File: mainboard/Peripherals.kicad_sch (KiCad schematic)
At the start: 30 parts, among them IC1101 PCAL6416AHF, IC1102 TMP100, IC1103 RV-8263-C8, IC506 PCA9306JK, Q1101 BSS138

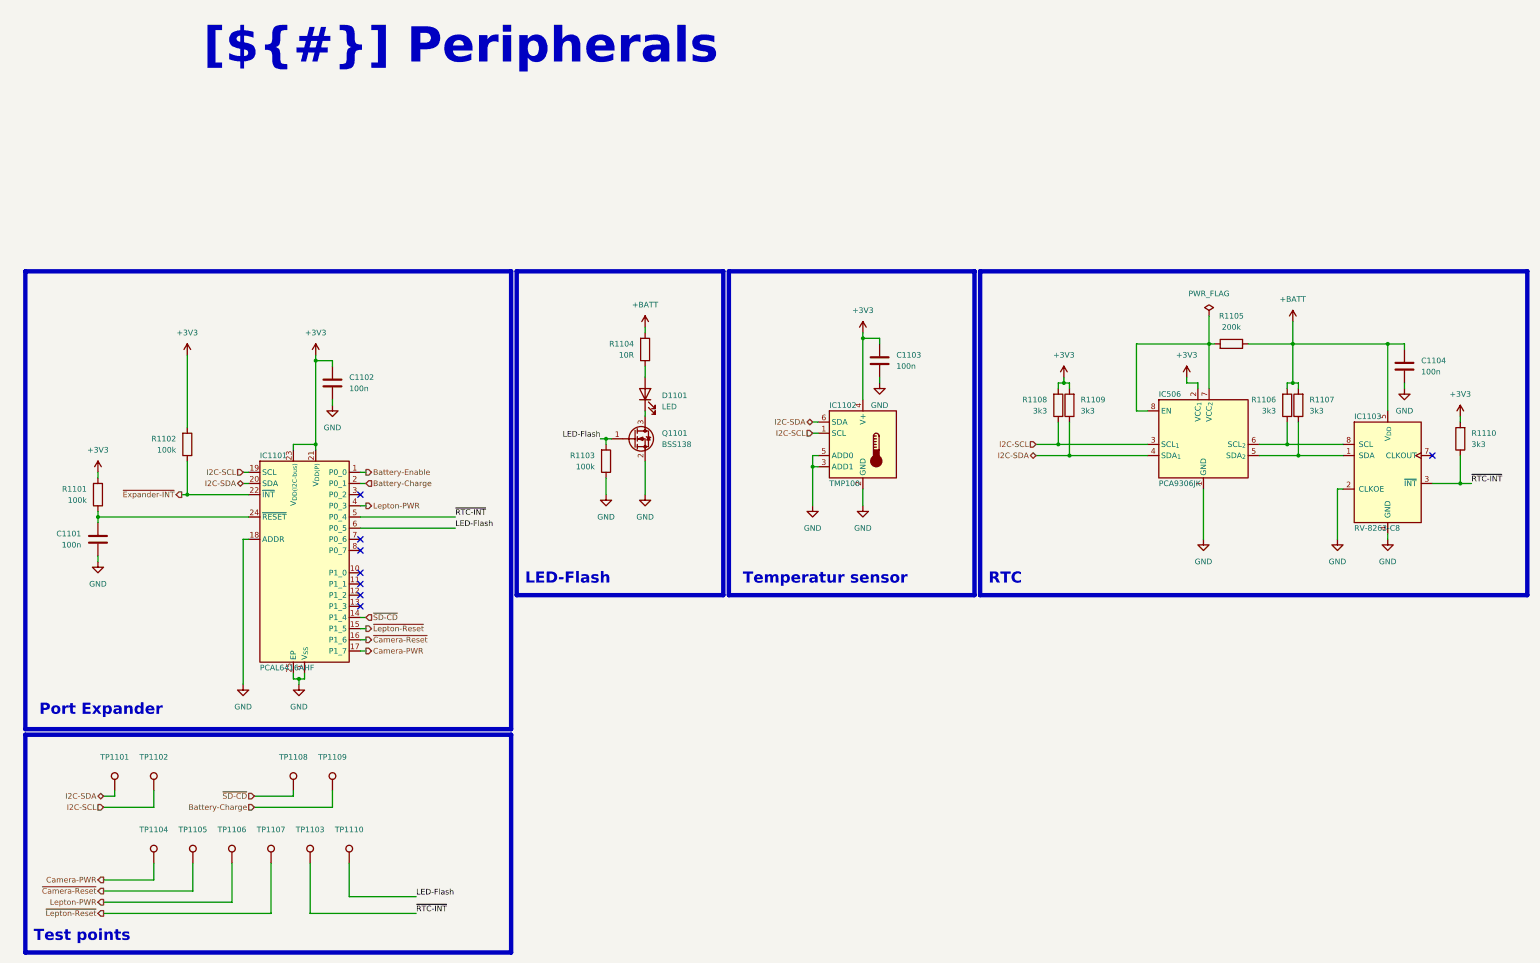
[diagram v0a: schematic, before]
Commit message: Continue routing, add flash LEDs for the RGB camera, add PWM controller for the Display Backlight and the flash LEDs, add Polyfuse for the battery
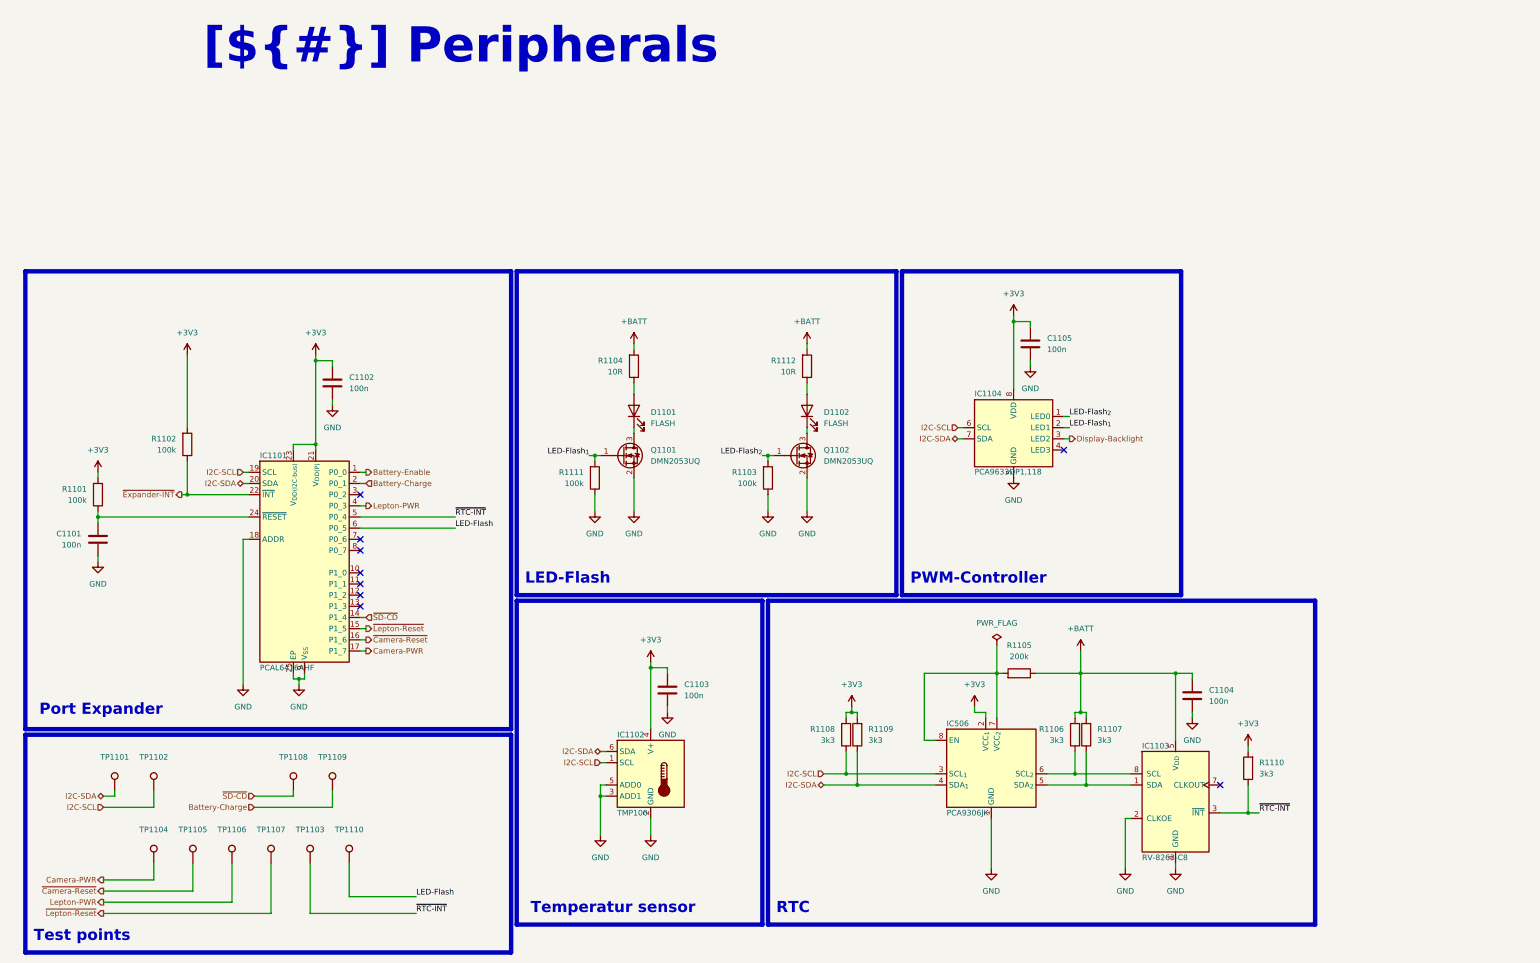
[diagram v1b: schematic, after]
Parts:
- removed Q1101: BSS138, Package_TO_SOT_SMD:SOT-23, symbol Transistor_FET:BSS138
- added C1105: 100n, Capacitor_SMD:C_0603_1608Metric, symbol Device:C
- added D1102: FLASH, LED_SMD:LED_Cree-XP-G, symbol Device:LED
- added IC1104: PCA9633DP1,118, Package_SO:TSSOP-8_3x3mm_P0.65mm, symbol NXP:PCA9633DP1,118
- added Q1101, Q1102: DMN2053UQ, Package_TO_SOT_SMD:SOT-23, symbol Diodes Incorporated:DMN2053UQ
- added R1111: 100k, Resistor_SMD:R_0603_1608Metric, symbol Device:R
- added R1112: 10R, Resistor_SMD:R_1206_3216Metric, symbol Device:R
- D1101: value LED -> FLASH; footprint (none) -> LED_SMD:LED_Cree-XP-G; manf (none) -> Cree LED; manf# (none) -> XPGDWT-BS-0000-00Q2E; mouser# (none) -> 941-PGDWTBS000000Q2E
- R1105: mouser# (none) -> 603-RC0603FR-07200KL
- R1106, R1107, R1108, R1109, R1110: mouser# (none) -> 603-RC0603FR-073K3L
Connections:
- net +3V3: now also C1105.1, IC1104.8 (VDD)
- net +BATT: now also R1112.2
- net GND: now also C1105.2, IC1104.5 (GND), Q1101.2 (S), Q1102.2 (S), R1111.1
- net I2C-SCL: now also IC1104.6 (SCL)
- net I2C-SDA: now also IC1104.7 (SDA)
- net LED-Flash: no longer R1103.2
- net at D1101.1 (K): now also Q1101.3 (D)
- new net: D1102.2 (A), R1112.1
- new net: D1102.1 (K), Q1102.3 (D)
- new net Display-Backlight: IC1104.3 (LED2)
- new net LED-Flash_{1}: IC1104.2 (LED1), Q1101.1 (G), R1111.2
- new net LED-Flash_{2}: IC1104.1 (LED0), Q1102.1 (G), R1103.2
- no-connect marks 8 -> 9
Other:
- moved on the sheet: C1103, C1104, D1101, IC1102, IC1103, IC506, R1103, R1104, R1105, R1106, R1107, R1108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

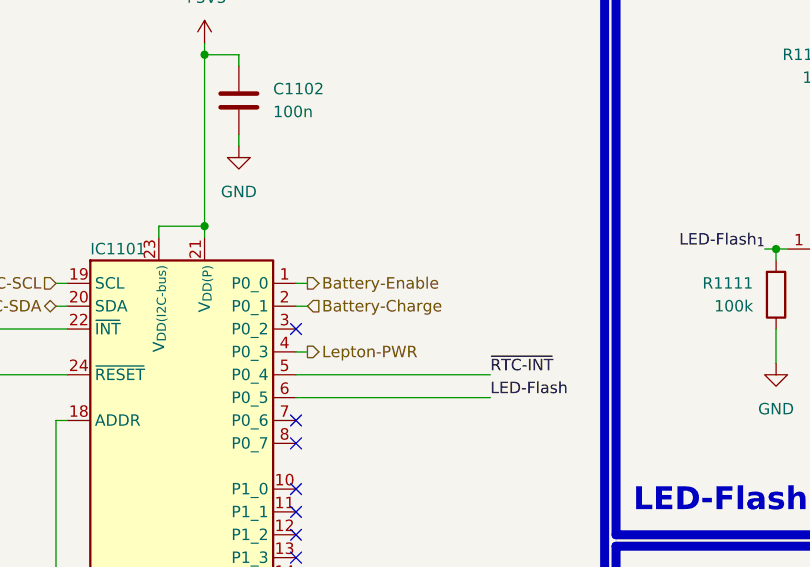
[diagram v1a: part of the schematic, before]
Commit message: Remove ADC for battery measurement and add a fuel gauge
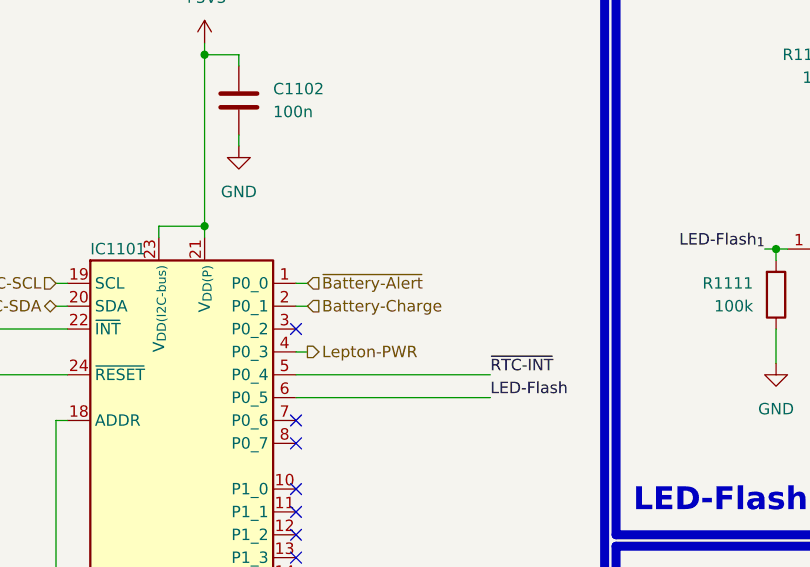
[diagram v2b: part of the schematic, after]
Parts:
- D1101, D1102: footprint LED_SMD:LED_Cree-XP-G -> Cree:XP-G
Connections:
- net Battery-Enable renamed ~{Battery-Alert}
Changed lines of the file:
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@@
 	(wire
 		(pts
-			(xy 125.73 116.84) (xy 127 116.84)
-		)
-		(stroke
-			(width 0)
-			(type default)
-		)
-	)
-	(wire
-		(pts
 			(xy 187.96 106.68) (xy 187.96 107.95)
 		)
@@
 	(wire
 		(pts
+			(xy 125.73 116.84) (xy 127 116.84)
+		)
+		(stroke
+			(width 0)
+			(type default)
+		)
+	)
+	(wire
+		(pts
 			(xy 85.09 121.92) (xy 86.36 121.92)
 		)
@@
 		)
 	)
+	(hierarchical_label "~{Battery-Alert}"
+		(shape input)
+		(at 127 116.84 0)
+		(effects
+			(font
+				(size 1.27 1.27)
+			)
+			(justify left)
+		)
+	)
 	(hierarchical_label "I2C-SCL"
 		(shape input)
@@
 		)
 	)
-	(hierarchical_label "Battery-Enable"
-		(shape output)
-		(at 127 116.84 0)
-		(effects
-			(font
-				(size 1.27 1.27)
-			)
-			(justify left)
-		)
-	)
 	(hierarchical_label "I2C-SDA"
 		(shape bidirectional)
@@
 			)
 		)
-		(property "Footprint" "LED_SMD:LED_Cree-XP-G"
+		(property "Footprint" "Cree:XP-G"
 			(at 187.96 102.87 0)
 			(effects
@@
 			)
 		)
-		(property "Footprint" "LED_SMD:LED_Cree-XP-G"
+		(property "Footprint" "Cree:XP-G"
 			(at 227.33 102.87 0)
 			(effects

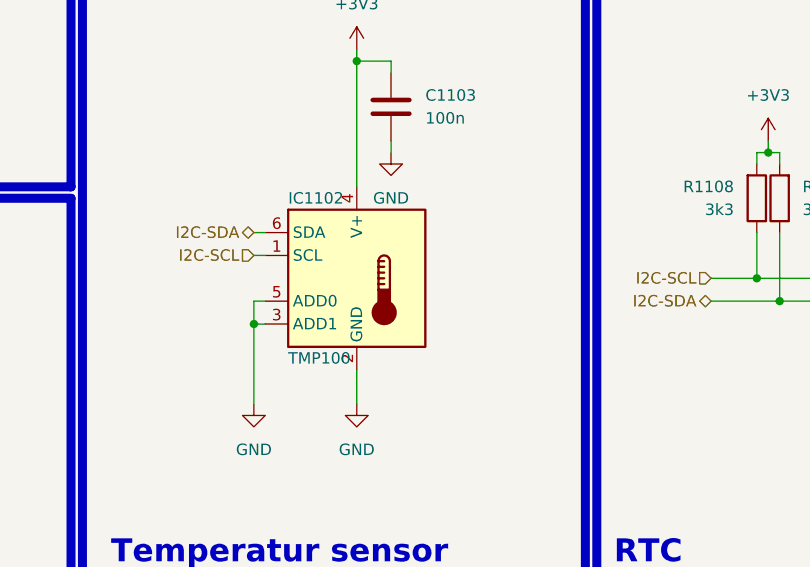
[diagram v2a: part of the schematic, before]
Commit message: Replace temperature sensor and optimize the position, replace LiPo battery with a flat one
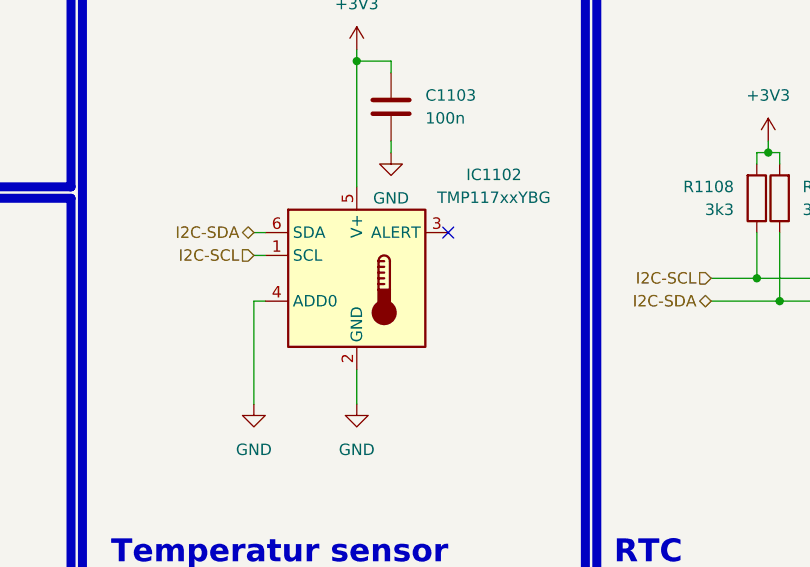
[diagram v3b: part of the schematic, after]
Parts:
- removed IC1102: TMP100, Package_TO_SOT_SMD:SOT-23-6, symbol Sensor_Temperature:TMP100
- added IC1102: TMP117xxYBG, Package_SON:WSON-6-1EP_2x2mm_P0.65mm_EP1x1.6mm, symbol Sensor_Temperature:TMP117xxDRV
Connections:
- net +3V3: now also IC1102.5 (V+)
- net GND: now also IC1102.2 (GND), IC1102.4 (ADD0)
- net I2C-SCL: now also IC1102.1 (SCL)
- net I2C-SDA: now also IC1102.6 (SDA)
- no-connect marks 9 -> 10

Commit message: Layout complete
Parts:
- renumbered C1105 to C1104, C1104 to C1105, IC506 to IC1103, IC1103 to IC1105, R1111 to R1103, R1103 to R1105, R1112 to R1106, R1108 to R1107, R1109 to R1108, R1105 to R1109, R1106 to R1110, R1107 to R1111, R1110 to R1112, TP1104 to TP1103, TP1105 to TP1104, TP1106 to TP1105, TP1107 to TP1106, TP1108 to TP1107, TP1103 to TP1108
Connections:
- net ~{Expander-INT} renamed ~{Expander-Int}
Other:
- moved on the sheet: C1101, C1102, C1104, C1105, IC1101, IC1103, IC1104, IC1105, R1101, R1102, R1107, R1108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

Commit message: Release 1.0.0
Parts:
- TP1101, TP1102, TP1103, TP1104, TP1105, TP1106, TP1107, TP1108, TP1109, TP1110: footprint TestPoint:TestPoint_Pad_1.0x1.0mm -> Testpoints_Kampi:TestPoint_Pad_1.0x1.0mm
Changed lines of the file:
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@@
 			)
 		)
-		(property "Footprint" "TestPoint:TestPoint_Pad_1.0x1.0mm"
+		(property "Footprint" "Testpoints_Kampi:TestPoint_Pad_1.0x1.0mm"
 			(at 83.82 205.74 0)
 			(effects
@@
 			)
 		)
-		(property "Footprint" "TestPoint:TestPoint_Pad_1.0x1.0mm"
+		(property "Footprint" "Testpoints_Kampi:TestPoint_Pad_1.0x1.0mm"
 			(at 128.27 205.74 0)
 			(effects
@@
 			)
 		)
-		(property "Footprint" "TestPoint:TestPoint_Pad_1.0x1.0mm"
+		(property "Footprint" "Testpoints_Kampi:TestPoint_Pad_1.0x1.0mm"
 			(at 92.71 205.74 0)
 			(effects
@@
 			)
 		)
-		(property "Footprint" "TestPoint:TestPoint_Pad_1.0x1.0mm"
+		(property "Footprint" "Testpoints_Kampi:TestPoint_Pad_1.0x1.0mm"
 			(at 101.6 205.74 0)
 			(effects
@@
 			)
 		)
-		(property "Footprint" "TestPoint:TestPoint_Pad_1.0x1.0mm"
+		(property "Footprint" "Testpoints_Kampi:TestPoint_Pad_1.0x1.0mm"
 			(at 83.82 189.23 0)
 			(effects
@@
 			)
 		)
-		(property "Footprint" "TestPoint:TestPoint_Pad_1.0x1.0mm"
+		(property "Footprint" "Testpoints_Kampi:TestPoint_Pad_1.0x1.0mm"
 			(at 115.57 189.23 0)
 			(effects
@@
 			)
 		)
-		(property "Footprint" "TestPoint:TestPoint_Pad_1.0x1.0mm"
+		(property "Footprint" "Testpoints_Kampi:TestPoint_Pad_1.0x1.0mm"
 			(at 124.46 189.23 0)
 			(effects
@@
 			)
 		)
-		(property "Footprint" "TestPoint:TestPoint_Pad_1.0x1.0mm"
+		(property "Footprint" "Testpoints_Kampi:TestPoint_Pad_1.0x1.0mm"
 			(at 110.49 205.74 0)
 			(effects
@@
 			)
 		)
-		(property "Footprint" "TestPoint:TestPoint_Pad_1.0x1.0mm"
+		(property "Footprint" "Testpoints_Kampi:TestPoint_Pad_1.0x1.0mm"
 			(at 64.77 189.23 0)
 			(effects
@@
 			)
 		)
-		(property "Footprint" "TestPoint:TestPoint_Pad_1.0x1.0mm"
+		(property "Footprint" "Testpoints_Kampi:TestPoint_Pad_1.0x1.0mm"
 			(at 119.38 205.74 0)
 			(effects

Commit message: Task: Issue #7
- Increase the width of the cutout for the temperature sensor
- Add missing component informations
- Fix wrong component informations

Closes: #7

Signed-off-by: Daniel Kampert <DanielKampert@kampis-elektroecke.de>
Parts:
- R1109: manf# RC0603FR-07200KL -> RC0603FR-073K3L
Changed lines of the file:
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@@
 			)
 		)
-		(property "manf#" "RC0603FR-07200KL"
+		(property "manf#" "RC0603FR-073K3L"
 			(at 275.59 161.29 0)
 			(effects

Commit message: Add feedback from PCBWay
Signed-off-by: Daniel Kampert <DanielKampert@kampis-elektroecke.de>
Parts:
- Q1101, Q1102: manf# DMN2053UQ -> DMN2053UQ-7; mouser# 621-DMN2053UQ -> 621-DMN2053UQ-7
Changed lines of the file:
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@@
 			)
 		)
-		(property "manf#" "DMN2053UQ"
+		(property "manf#" "DMN2053UQ-7"
 			(at 224.79 113.03 0)
 			(effects
@@
 			)
 		)
-		(property "mouser#" "621-DMN2053UQ"
+		(property "mouser#" "621-DMN2053UQ-7"
 			(at 224.79 113.03 0)
 			(effects
@@
 			)
 		)
-		(property "manf#" "DMN2053UQ"
-			(at 185.42 113.03 0)
-			(effects
-				(font
-					(size 1.27 1.27)
-				)
-				(hide yes)
-			)
-		)
-		(property "mouser#" "621-DMN2053UQ"
-			(at 185.42 113.03 0)
-			(effects
+		(property "manf#" "DMN2053UQ-7"
+			(at 185.42 113.03 0)
+			(effects
+				(font
+					(size 1.27 1.27)
+				)
+				(hide yes)
+			)
+		)
+		(property "mouser#" "621-DMN2053UQ-7"
+			(at 185.42 113.03 0)
+			(effects

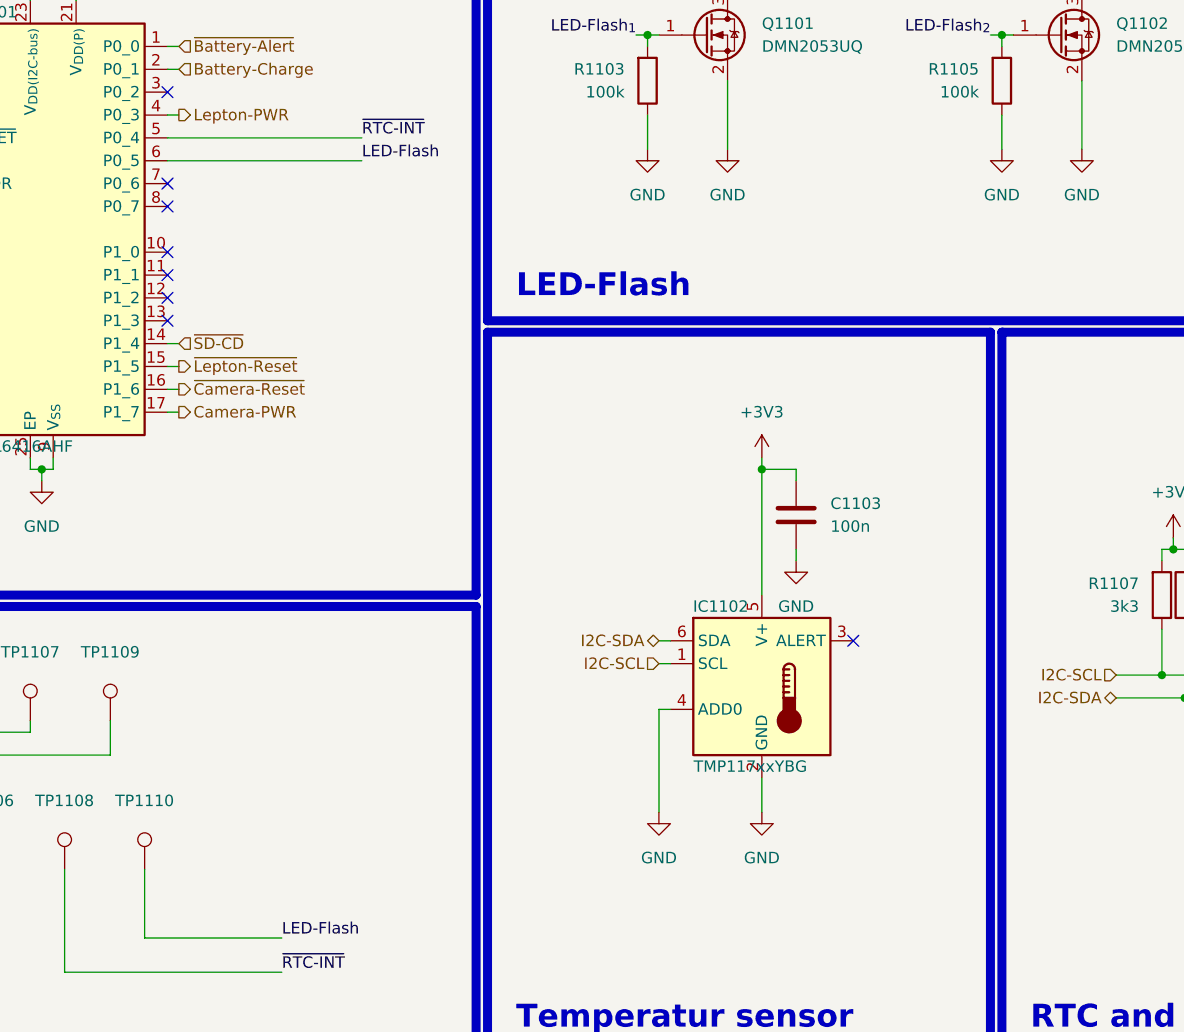
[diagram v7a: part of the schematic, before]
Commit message: Feature: Issue #21
- Connect the TMP117 temperatur alert pin
- Add CI/CD workflow to check for changelog updates on pull requests

Closes #21

Signed-off-by: Daniel Kampert <DanielKampert@kampis-elektroecke.de>
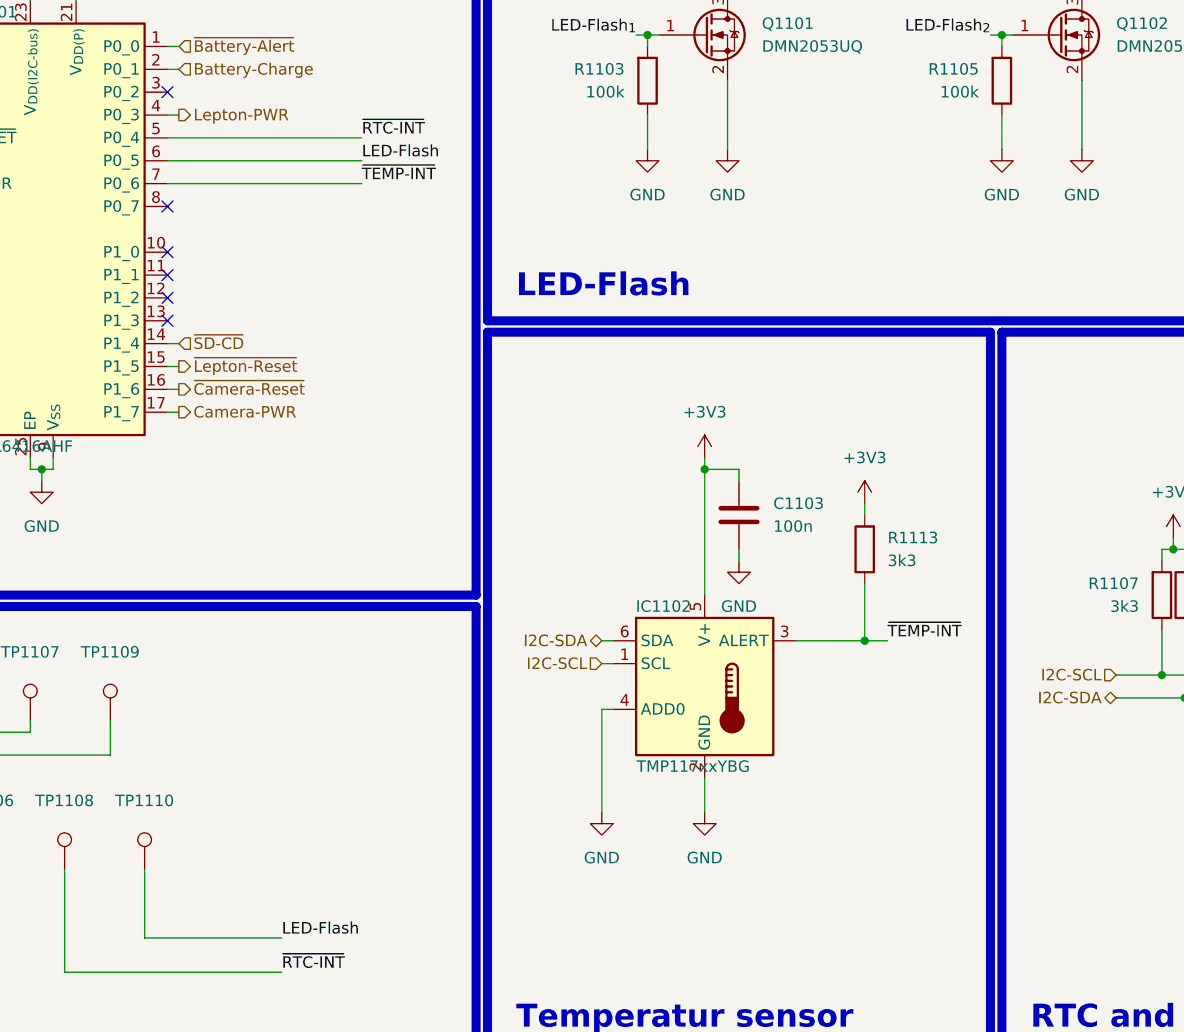
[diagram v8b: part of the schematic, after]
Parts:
- added R1113: 3k3, Resistor_SMD:R_0603_1608Metric, symbol Device:R
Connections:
- net +3V3: now also R1113.2
- net ~{TEMP-INT}: now reaches IC1102.3 (ALERT)
- net ~{TEMP-INT}: now also IC1101.7 (P0_6), R1113.1
- no-connect marks 10 -> 8
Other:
- moved on the sheet: C1103, IC1102
